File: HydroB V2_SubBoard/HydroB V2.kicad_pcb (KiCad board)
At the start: 4 copper layers, 106.8 x 81.2 mm, 122 parts, among them J10 Screw_Terminal_01x02, J16 Screw_Terminal_01x02, J3 Screw_Terminal_01x02, J4 Conn_01x04_Pin, J5 PH SENSOR, J6 EC SENSOR, J7 Conn_01x02_Pin, J8 Screw_Terminal_01x02, J9 Screw_Terminal_01x02, Q1 S8050, Q2 S8050, Q3 S8050, Q4 S8050, Q5 S8050, SW1 SW_Push, U1 STM32F103C8Tx, U3 SN65HVD72DR, U4 LMR33620ADDA, Y1 8Mhz

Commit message: PCB update
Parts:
- removed G***: LOGO, CHIPTREE_LOGO:cam5x5
- removed G***: LOGO, CHIPTREE_LOGO:CHPTREE-5x5mm
- removed PS2: HLK-20M12, Converter_ACDC:Converter_ACDC_Hi-Link_HLK-20Mxx
- removed kibuzzard-668BA666: G***, kibuzzard-668BA666
- removed kibuzzard-668BA6B4: G***, kibuzzard-668BA6B4
- removed kibuzzard-668BA6C7: G***, kibuzzard-668BA6C7
- removed kibuzzard-668BA6F1: G***, kibuzzard-668BA6F1
- removed kibuzzard-668BA7A5: G***, kibuzzard-668BA7A5
- removed kibuzzard-668BA7C8: G***, kibuzzard-668BA7C8
- removed kibuzzard-668BA7EF: G***, kibuzzard-668BA7EF
- removed kibuzzard-668BA811: G***, kibuzzard-668BA811
- removed kibuzzard-668BA833: G***, kibuzzard-668BA833
- removed kibuzzard-668BA852: G***, kibuzzard-668BA852
- removed kibuzzard-668BA86D: G***, kibuzzard-668BA86D
- removed kibuzzard-668BA998 (x2): G***, kibuzzard-668BA998
- removed kibuzzard-668BA9FB (x2): G***, kibuzzard-668BA9FB
- removed kibuzzard-668BAA24 (x2): G***, kibuzzard-668BAA24
- removed kibuzzard-668BAA39 (x2): G***, kibuzzard-668BAA39
- removed kibuzzard-668BAA96 (x5): G***, kibuzzard-668BAA96
- removed kibuzzard-668BAD03 (x5): G***, kibuzzard-668BAD03
- added D15: D_TVS, Diode_SMD:D_SOD-123F, F.Cu at (124.2, 65.0)
- added D16: LED_Small, LED_SMD:LED_0805_2012Metric, F.Cu at (159.0, 59.7)
- added D17: LED_Small, LED_SMD:LED_0805_2012Metric, F.Cu at (163.4, 59.7)
- added J1: Conn_01x02_Pin, Connector_Phoenix_MC:PhoenixContact_MCV_1,5_2-G-3.81_1x02_P3.81mm_Vertical, F.Cu at (117.8, 61.1)
- added J2: 12V, Connector_BarrelJack:BarrelJack_Horizontal, F.Cu at (176.2, 78.4)
- added Q6: S8050, Package_TO_SOT_SMD:SOT-23, F.Cu at (129.6, 58.2)
- added Q7: S8050, Package_TO_SOT_SMD:SOT-23, F.Cu at (141.2, 58.1)
- added R29: 1k, Resistor_SMD:R_0603_1608Metric, F.Cu at (156.9, 59.7)
- added R30: 1k, Resistor_SMD:R_0603_1608Metric, F.Cu at (161.3, 59.7)
- added R31: 1K, Resistor_SMD:R_0603_1608Metric, F.Cu at (125.8, 59.2)
- added R32: 10K, Resistor_SMD:R_0603_1608Metric, F.Cu at (125.8, 57.2)
- added R33: 1K, Resistor_SMD:R_0603_1608Metric, F.Cu at (145.0, 59.1)
- added R34: 10K, Resistor_SMD:R_0603_1608Metric, F.Cu at (145.0, 57.2)
- added kibuzzard-669F2037: G***, kibuzzard-669F2037, F.Cu at (135.4, 59.0)
- added kibuzzard-669F208D: G***, kibuzzard-669F208D, F.Cu at (137.5, 62.0)
- added kibuzzard-669F20C5: G***, kibuzzard-669F20C5, F.Cu at (133.4, 62.0)
- added kibuzzard-669F20DD: G***, kibuzzard-669F20DD, F.Cu at (148.1, 57.5)
- added kibuzzard-669F20FF: G***, kibuzzard-669F20FF, F.Cu at (150.1, 57.7)
- added kibuzzard-669F211D: G***, kibuzzard-669F211D, F.Cu at (152.1, 57.5)
- added kibuzzard-669F2125: G***, kibuzzard-669F2125, F.Cu at (154.1, 57.5)
- added kibuzzard-669F24DA: G***, kibuzzard-669F24DA, F.Cu at (157.9, 57.1)
- added kibuzzard-669F24EA: G***, kibuzzard-669F24EA, F.Cu at (162.3, 57.0)
- added kibuzzard-669F2500: G***, kibuzzard-669F2500, F.Cu at (167.0, 59.5)
- added kibuzzard-669F250D: G***, kibuzzard-669F250D, F.Cu at (183.1, 66.6)
- added kibuzzard-669F251A: G***, kibuzzard-669F251A, F.Cu at (143.7, 73.9)
- added kibuzzard-669F255D: G***, kibuzzard-669F255D, F.Cu at (123.5, 72.9)
- added kibuzzard-669F2571: G***, kibuzzard-669F2571, F.Cu at (123.4, 78.4)
- added kibuzzard-669F2588: G***, kibuzzard-669F2588, F.Cu at (117.8, 56.9)
- added kibuzzard-669F2592: G***, kibuzzard-669F2592, F.Cu at (114.0, 57.0)
- added kibuzzard-669F259B: G***, kibuzzard-669F259B, F.Cu at (101.4, 67.2)
- added kibuzzard-669F25AE: G***, kibuzzard-669F25AE, F.Cu at (101.4, 71.0)
- added kibuzzard-669F25B6: G***, kibuzzard-669F25B6, F.Cu at (101.4, 74.8)
- added kibuzzard-669F25BD: G***, kibuzzard-669F25BD, F.Cu at (101.4, 78.6)
- added kibuzzard-669F25C8: G***, kibuzzard-669F25C8, F.Cu at (108.8, 121.2)
- added kibuzzard-669F25D3: G***, kibuzzard-669F25D3, F.Cu at (113.8, 121.3)
- added kibuzzard-669F25DA: G***, kibuzzard-669F25DA, F.Cu at (124.3, 121.3)
- added kibuzzard-669F25E1: G***, kibuzzard-669F25E1, F.Cu at (129.3, 121.3)
- added kibuzzard-669F25EE: G***, kibuzzard-669F25EE, F.Cu at (139.6, 121.4)
- added kibuzzard-669F25F4: G***, kibuzzard-669F25F4, F.Cu at (144.6, 121.5)
- added kibuzzard-669F25FE: G***, kibuzzard-669F25FE, F.Cu at (155.1, 121.4)
- added kibuzzard-669F2610: G***, kibuzzard-669F2610, F.Cu at (160.1, 121.5)
- added kibuzzard-669F261C: G***, kibuzzard-669F261C, F.Cu at (170.7, 121.4)
- added kibuzzard-669F2622: G***, kibuzzard-669F2622, F.Cu at (175.7, 121.5)
- J4: footprint Connector_JST:JST_XH_B4B-XH-A_1x04_P2.50mm_Vertical -> Connector_PinHeader_2.00mm:PinHeader_1x04_P2.00mm_Vertical
- J5: value PH SENSOR -> Conn_01x02_Pin; footprint Connector_Phoenix_MC:PhoenixContact_MCV_1,5_4-G-3.81_1x04_P3.81mm_Vertical -> Connector_PinHeader_2.00mm:PinHeader_1x02_P2.00mm_Vertical
- J6: value EC SENSOR -> SENSOR
- J7: footprint Connector_Phoenix_MC:PhoenixContact_MCV_1,5_2-G-3.81_1x02_P3.81mm_Vertical -> Connector_PinHeader_2.00mm:PinHeader_1x02_P2.00mm_Vertical
- L2: footprint Inductor_SMD:L_Bourns-SRN4018 -> Inductor_SMD:L_Bourns_SRP5030T
- moved H6 120.7 mm to (104.2, 59.7)
- moved H8 99.7 mm to (180.4, 118.7)
- moved J4 79.6 mm to (148.1, 60.5)
- moved J7 74.7 mm to (137.5, 57.9), turned to 0 degrees
- moved SW1 70.3 mm to (179.4, 64.4), turned to -90 degrees
- moved C29 66.4 mm to (168.5, 77.8), turned to 90 degrees
- moved D4 64.8 mm to (166.1, 61.9)
- moved R20 64.5 mm to (168.2, 61.9)
- moved C28 63.2 mm to (165.5, 77.8), turned to 90 degrees
- moved C9 61.9 mm to (168.7, 72.0), turned to 0 degrees
- moved J3 61.5 mm to (108.8, 115.3), turned to 0 degrees
- moved C27 60.0 mm to (162.5, 77.8), turned to 90 degrees
- moved R18 59.7 mm to (111.9, 86.5)
- moved R9 59.7 mm to (111.9, 84.5)
- moved D2 59.7 mm to (109.9, 89.8)
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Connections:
- J5 pad 1: GND -> +12V
- J6 pad 2: Net-(J5-Pin_2) -> Net-(D15-A1)
- J6 pad 3: Net-(J5-Pin_3) -> Net-(D15-A2)
- J7 pad 1: N -> +12V
- J7 pad 2: L -> Net-(J7-Pin_2)
- R10 pad 2: Net-(J5-Pin_2) -> Net-(D15-A1)
- R15 pad 1: Net-(J5-Pin_2) -> Net-(D15-A1)
- R15 pad 2: Net-(J5-Pin_3) -> Net-(D15-A2)
- R4 pad 1: Net-(J5-Pin_3) -> Net-(D15-A2)
- R5 pad 1: Net-(J5-Pin_2) -> Net-(D15-A1)
- R5 pad 2: Net-(J5-Pin_3) -> Net-(D15-A2)
- U1 pad 12: /HydroB/Block Relay1/RELAY_3 -> unconnected-(U1-PA2-Pad12)
- U1 pad 13: /HydroB/Block Relay1/RELAY_2 -> unconnected-(U1-PA3-Pad13)
- U1 pad 15: /HydroB/Block Relay1/RELAY_1 -> unconnected-(U1-PA5-Pad15)
- U1 pad 16: unconnected-(U1-PA6-Pad16) -> LED2
- U1 pad 17: /HydroB/Block Relay1/RELAY_5 -> LED1
- U1 pad 32: unconnected-(U1-PA11-Pad32) -> /HydroB/Block Relay1/RELAY_1
- U1 pad 33: unconnected-(U1-PA12-Pad33) -> /HydroB/Block Relay1/RELAY_2
- U1 pad 38: unconnected-(U1-PA15-Pad38) -> /HydroB/Block Relay1/RELAY_3
- U1 pad 39: unconnected-(U1-PB3-Pad39) -> /HydroB/Block Relay1/RELAY_4
- U1 pad 40: unconnected-(U1-PB4-Pad40) -> /HydroB/Block Relay1/RELAY_5
- U1 pad 46: /HydroB/Block Relay1/RELAY_4 -> unconnected-(U1-PB9-Pad46)
- U3 pad 6: Net-(J5-Pin_2) -> Net-(D15-A1)
- U3 pad 7: Net-(J5-Pin_3) -> Net-(D15-A2)
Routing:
- net Net-(J5-Pin_3): track 93.9 -> 0.00 mm, vias 1 -> 0
- net Net-(J5-Pin_2): track 83.3 -> 4.28 mm, vias 1 -> 0
- net +3.3V: track 90.6 -> 31.3 mm, vias 42 -> 61
- net Net-(D15-A1): track 0.00 -> 54.8 mm
- net Net-(D15-A2): track 0.00 -> 52.8 mm
- net SWCLK: track 86.1 -> 38.9 mm
- net +12V: track 0.00 -> 41.1 mm, vias 42 -> 46
- net SWDIO: track 85.7 -> 46.3 mm
- net LED2: track 0.00 -> 30.9 mm
- net PG: track 30.0 -> 3.10 mm
- net /HydroB/Block Relay1/RELAY_1: track 46.0 -> 27.2 mm
- net /HydroB/Block Relay1/RELAY_5: track 63.8 -> 46.1 mm
- net /HydroB/Block Relay1/RELAY_2: track 28.8 -> 11.2 mm
- net LED1: track 0.00 -> 16.7 mm
- net NRST: track 52.9 -> 68.2 mm, vias 1 -> 0
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- added copper zone on F.Cu, net A
- removed copper zone on F.Cu, net L
- removed copper zone on F.Cu, net N
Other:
- board size 106.8 x 81.2 mm -> 83.4 x 66.2 mm
- board text removed: "HYDRO-B"

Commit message: new update
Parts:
- removed kibuzzard-669F2037: G***, kibuzzard-669F2037
- added kibuzzard-66A1D076: G***, kibuzzard-66A1D076, F.Cu at (135.4, 58.8)
- moved R25 0.33 mm to (120.4, 85.2)
- moved R26 0.25 mm to (137.6, 85.2)
- moved R17 0.18 mm to (122.3, 70.4)
- moved R21 0.12 mm to (122.4, 75.9)
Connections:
- J5 pad 1: +12V -> +3.3V
- J7 pad 1: +12V -> +3.3V
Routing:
- net +3.3V: track 31.3 -> 92.1 mm, vias 61 -> 62
- net +12V: track 41.1 -> 0.00 mm

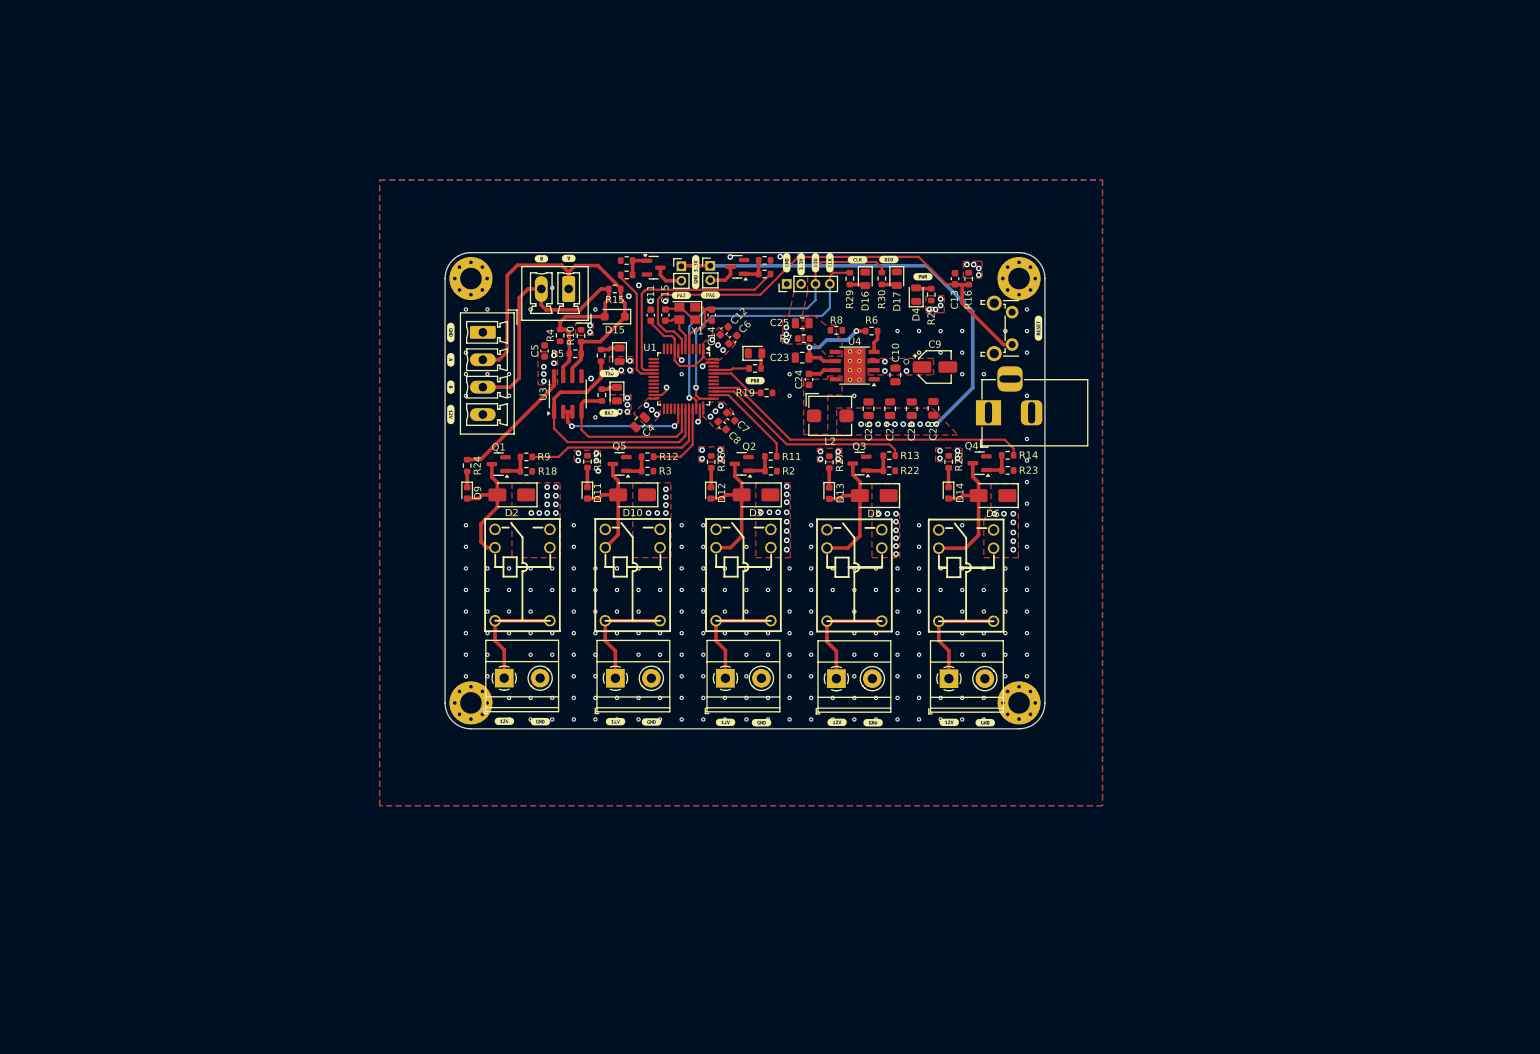
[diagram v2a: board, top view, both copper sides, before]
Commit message: PCB component placement and layout
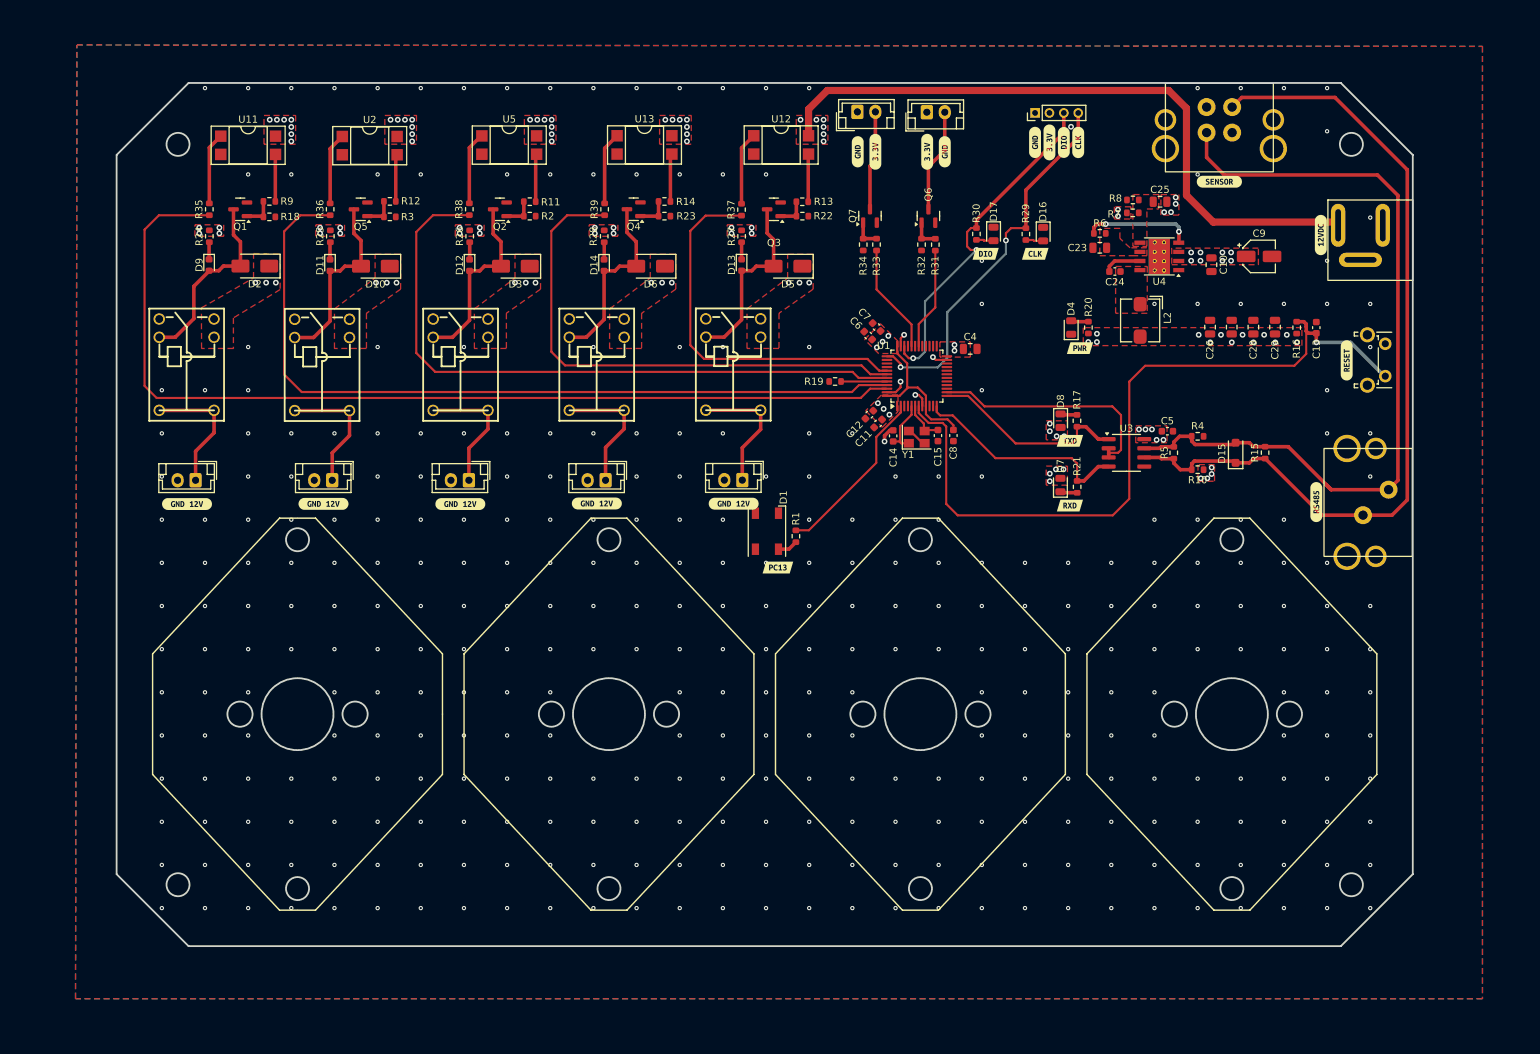
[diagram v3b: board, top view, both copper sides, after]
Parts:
- removed H5, H6, H7, H8: MountingHole, MountingHole:MountingHole_3mm_Pad_Via
- removed kibuzzard-669F208D: G***, kibuzzard-669F208D
- removed kibuzzard-669F20C5: G***, kibuzzard-669F20C5
- removed kibuzzard-669F20DD: G***, kibuzzard-669F20DD
- removed kibuzzard-669F20FF: G***, kibuzzard-669F20FF
- removed kibuzzard-669F211D: G***, kibuzzard-669F211D
- removed kibuzzard-669F2125: G***, kibuzzard-669F2125
- removed kibuzzard-669F24DA: G***, kibuzzard-669F24DA
- removed kibuzzard-669F24EA: G***, kibuzzard-669F24EA
- removed kibuzzard-669F2500: G***, kibuzzard-669F2500
- removed kibuzzard-669F250D: G***, kibuzzard-669F250D
- removed kibuzzard-669F251A: G***, kibuzzard-669F251A
- removed kibuzzard-669F255D: G***, kibuzzard-669F255D
- removed kibuzzard-669F2571: G***, kibuzzard-669F2571
- removed kibuzzard-669F2588: G***, kibuzzard-669F2588
- removed kibuzzard-669F2592: G***, kibuzzard-669F2592
- removed kibuzzard-669F259B: G***, kibuzzard-669F259B
- removed kibuzzard-669F25AE: G***, kibuzzard-669F25AE
- removed kibuzzard-669F25B6: G***, kibuzzard-669F25B6
- removed kibuzzard-669F25BD: G***, kibuzzard-669F25BD
- removed kibuzzard-669F25C8: G***, kibuzzard-669F25C8
- removed kibuzzard-669F25D3: G***, kibuzzard-669F25D3
- removed kibuzzard-669F25DA: G***, kibuzzard-669F25DA
- removed kibuzzard-669F25E1: G***, kibuzzard-669F25E1
- removed kibuzzard-669F25EE: G***, kibuzzard-669F25EE
- removed kibuzzard-669F25F4: G***, kibuzzard-669F25F4
- removed kibuzzard-669F25FE: G***, kibuzzard-669F25FE
- removed kibuzzard-669F2610: G***, kibuzzard-669F2610
- removed kibuzzard-669F261C: G***, kibuzzard-669F261C
- removed kibuzzard-669F2622: G***, kibuzzard-669F2622
- removed kibuzzard-66A1D076: G***, kibuzzard-66A1D076
- added R35: 220R, Resistor_SMD:R_0603_1608Metric, F.Cu at (67.8, 50.1)
- added R36: 220R, Resistor_SMD:R_0603_1608Metric, F.Cu at (84.6, 50.1)
- added R37: 220R, Resistor_SMD:R_0603_1608Metric, F.Cu at (141.8, 50.1)
- added R38: 220R, Resistor_SMD:R_0603_1608Metric, F.Cu at (104.0, 50.1)
- added R39: 220R, Resistor_SMD:R_0603_1608Metric, F.Cu at (122.8, 50.1)
- added U11: PC817, Package_DIP:DIP-4_W7.62mm_SMDSocket_SmallPads, F.Cu at (73.2, 41.2)
- added U12: PC817, Package_DIP:DIP-4_W7.62mm_SMDSocket_SmallPads, F.Cu at (147.3, 41.1)
- added U13: PC817, Package_DIP:DIP-4_W7.62mm_SMDSocket_SmallPads, F.Cu at (128.3, 41.1)
- added U2: PC817, Package_DIP:DIP-4_W7.62mm_SMDSocket_SmallPads, F.Cu at (90.1, 41.2)
- added U5: PC817, Package_DIP:DIP-4_W7.62mm_SMDSocket_SmallPads, F.Cu at (109.5, 41.1)
- added kibuzzard-66A86A88: G***, kibuzzard-66A86A88, F.Cu at (170.1, 42.1)
- added kibuzzard-66A86A88: G***, kibuzzard-66A86A88, F.Cu at (158.0, 42.1)
- added kibuzzard-66A86A88: G***, kibuzzard-66A86A88, F.Cu at (182.6, 40.8)
- added kibuzzard-66A86AEA: G***, kibuzzard-66A86AEA, F.Cu at (225.9, 71.1)
- added kibuzzard-66A86B8E: G***, kibuzzard-66A86B8E, F.Cu at (167.6, 42.1)
- added kibuzzard-66A86B8E: G***, kibuzzard-66A86B8E, F.Cu at (184.6, 40.8)
- added kibuzzard-66A86B8E: G***, kibuzzard-66A86B8E, F.Cu at (160.4, 42.1)
- added kibuzzard-66A86BAD: G***, kibuzzard-66A86BAD, F.Cu at (186.6, 40.8)
- added kibuzzard-66A86BBB: G***, kibuzzard-66A86BBB, F.Cu at (188.6, 40.8)
- added kibuzzard-66A8B27E: G***, kibuzzard-66A8B27E, F.Cu at (208.2, 46.2)
- added kibuzzard-66A8B2A7: G***, kibuzzard-66A8B2A7, F.Cu at (221.7, 90.8)
- added kibuzzard-66AAEFF5: G***, kibuzzard-66AAEFF5, F.Cu at (121.7, 91.0)
- added kibuzzard-66AAEFF5: G***, kibuzzard-66AAEFF5, F.Cu at (64.7, 91.0)
- added kibuzzard-66AAEFF5: G***, kibuzzard-66AAEFF5, F.Cu at (102.7, 91.0)
- added kibuzzard-66AAEFF5: G***, kibuzzard-66AAEFF5, F.Cu at (83.7, 91.0)
- added kibuzzard-66AAEFF5: G***, kibuzzard-66AAEFF5, F.Cu at (140.7, 91.0)
- added kibuzzard-66AAF0AE: G***, kibuzzard-66AAF0AE, F.Cu at (146.9, 99.9)
- added kibuzzard-66AAF0BB: G***, kibuzzard-66AAF0BB, F.Cu at (187.5, 91.3)
- added kibuzzard-66AAF0C8: G***, kibuzzard-66AAF0C8, F.Cu at (187.5, 82.3)
- added kibuzzard-66AAF0D5: G***, kibuzzard-66AAF0D5, F.Cu at (188.9, 69.4)
- added kibuzzard-66AAF0E0: G***, kibuzzard-66AAF0E0, F.Cu at (182.7, 56.3)
- added kibuzzard-66AAF0E8: G***, kibuzzard-66AAF0E8, F.Cu at (175.8, 56.3)
- added kibuzzard-66AAF2E3: G***, kibuzzard-66AAF2E3, F.Cu at (222.3, 53.6)
- D1: footprint LED_SMD:LED_0805_2012Metric -> LED_SMD:LED_Cree-PLCC4_5x5mm_CW
- J1: footprint Connector_Phoenix_MC:PhoenixContact_MCV_1,5_2-G-3.81_1x02_P3.81mm_Vertical -> hydroB:Din sensor
- J10, J16, J3, J8, J9: footprint TerminalBlock_Phoenix:TerminalBlock_Phoenix_MKDS-1,5-2_1x02_P5.00mm_Horizontal -> Connector_JST:JST_EH_B2B-EH-A_1x02_P2.50mm_Vertical
- J2: footprint Connector_BarrelJack:BarrelJack_Horizontal -> Library:DC conn
- J5, J7: footprint Connector_PinHeader_2.00mm:PinHeader_1x02_P2.00mm_Vertical -> Connector_JST:JST_EH_B2B-EH-A_1x02_P2.50mm_Vertical
- J6: footprint Connector_Phoenix_MC:PhoenixContact_MCV_1,5_4-G-3.81_1x04_P3.81mm_Vertical -> hydroB:Din sensor 4 Pin
- moved J1 121.0 mm to (235.1, 90.8), turned to -90 degrees
- moved J6 108.2 mm to (208.2, 32.2), turned to 0 degrees
- moved R15 93.2 mm to (214.6, 83.9), turned to 90 degrees
- moved R4 89.7 mm to (205.2, 81.6), turned to 0 degrees
- moved D15 88.4 mm to (210.5, 83.9), turned to 90 degrees
- moved R10 87.7 mm to (205.2, 86.3), turned to 180 degrees
- moved C5 87.3 mm to (201.0, 80.9), turned to 0 degrees
- moved R5 84.3 mm to (201.9, 83.9), turned to 90 degrees
- moved U3 78.1 mm to (195.3, 83.9), turned to 0 degrees
- moved R21 67.3 mm to (188.5, 88.7), turned to -90 degrees
- moved R17 66.8 mm to (188.4, 79.5)
- moved D7 62.9 mm to (186.2, 88.4), turned to 90 degrees
- moved J2 62.8 mm to (231.0, 47.7), turned to 0 degrees
- moved D8 62.0 mm to (186.2, 79.5)
- moved Q4 59.7 mm to (126.8, 50.1)
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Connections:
- net A renamed /HydroB/Power Supply1/SW
- R11 pad 1: /HydroB/Block Relay1/RELAY_3 -> Net-(R11-Pad1)
- R12 pad 1: /HydroB/Block Relay1/RELAY_2 -> Net-(R12-Pad1)
- R13 pad 1: /HydroB/Block Relay1/RELAY_4 -> Net-(R13-Pad1)
- R14 pad 1: /HydroB/Block Relay1/RELAY_5 -> Net-(R14-Pad1)
- R9 pad 1: /HydroB/Block Relay1/RELAY_1 -> Net-(R9-Pad1)
- U1 pad 12: unconnected-(U1-PA2-Pad12) -> /HydroB/Block Sensor1/RS485_RX
- U1 pad 13: unconnected-(U1-PA3-Pad13) -> /HydroB/Block Sensor1/RS485_TX
- U1 pad 14: unconnected-(U1-PA4-Pad14) -> /HydroB/Block Sensor1/EN_RS485
- U1 pad 16: LED2 -> unconnected-(U1-PA6-Pad16)
- U1 pad 17: LED1 -> unconnected-(U1-PA7-Pad17)
- U1 pad 2: unconnected-(U1-PC13-Pad2) -> LED
- U1 pad 29: /HydroB/Block Sensor1/EN_RS485 -> unconnected-(U1-PA8-Pad29)
- U1 pad 30: /HydroB/Block Sensor1/RS485_RX -> LED1
- U1 pad 31: /HydroB/Block Sensor1/RS485_TX -> unconnected-(U1-PA10-Pad31)
- U1 pad 32: /HydroB/Block Relay1/RELAY_1 -> LED2
- U1 pad 33: /HydroB/Block Relay1/RELAY_2 -> unconnected-(U1-PA12-Pad33)
- U1 pad 38: /HydroB/Block Relay1/RELAY_3 -> unconnected-(U1-PA15-Pad38)
- U1 pad 39: /HydroB/Block Relay1/RELAY_4 -> unconnected-(U1-PB3-Pad39)
- U1 pad 40: /HydroB/Block Relay1/RELAY_5 -> unconnected-(U1-PB4-Pad40)
- U1 pad 41: unconnected-(U1-PB5-Pad41) -> /HydroB/Block Relay1/RELAY_4
- U1 pad 42: unconnected-(U1-PB6-Pad42) -> /HydroB/Block Relay1/RELAY_5
- U1 pad 43: unconnected-(U1-PB7-Pad43) -> /HydroB/Block Relay1/RELAY_3
- U1 pad 45: LED -> /HydroB/Block Relay1/RELAY_2
- U1 pad 46: unconnected-(U1-PB9-Pad46) -> /HydroB/Block Relay1/RELAY_1
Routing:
- net /HydroB/Block Relay1/RELAY_1: track 27.2 -> 135.9 mm
- net /HydroB/Block Relay1/RELAY_2: track 11.2 -> 112.4 mm
- net +12V: track 0.00 -> 93.1 mm, vias 46 -> 57
- net /HydroB/Block Relay1/RELAY_3: track 13.4 -> 92.0 mm
- net +3.3V: track 92.1 -> 20.4 mm, vias 62 -> 64
- net Net-(D15-A1): track 54.6 -> 118.1 mm
- net Net-(D15-A2): track 52.8 -> 113.4 mm
- net NRST: track 68.1 -> 106.8 mm, vias 0 -> 1
- net /HydroB/Block Relay1/RELAY_5: track 46.1 -> 73.1 mm
- net /HydroB/Block Relay1/RELAY_4: track 29.4 -> 52.7 mm
- net LED: track 5.02 -> 24.4 mm
- net LED2: track 31.1 -> 15.3 mm
- net Net-(U4-VCC): track 14.0 -> 0.00 mm, vias 2 -> 0
- net SWCLK: track 38.9 -> 52.6 mm, vias 1 -> 2
- net /HydroB/Block Sensor1/EN_RS485: track 20.4 -> 33.6 mm, vias 2 -> 0
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- added copper zone on F.Cu, net Net-(U4-VCC)
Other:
- board size 83.4 x 66.2 mm -> 180.2 x 120 mm
